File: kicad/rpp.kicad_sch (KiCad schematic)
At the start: 13 parts, among them J1 SolderPad, J2 SolderPad, J3 SolderPad, J4 SolderPad, Q1 CSD19537Q3, U1 LM5050-1

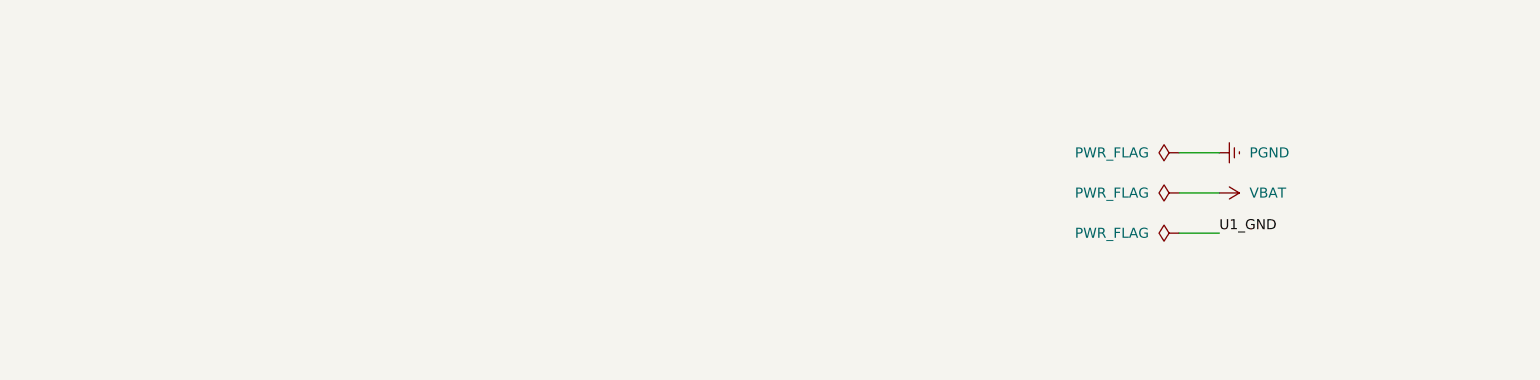
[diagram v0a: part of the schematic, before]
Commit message: Adjusted licensing for club
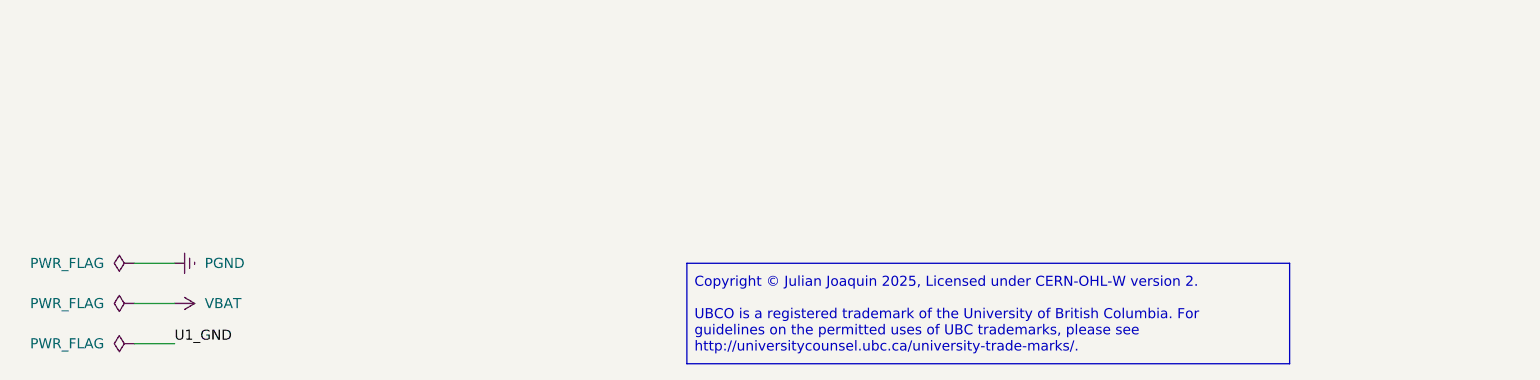
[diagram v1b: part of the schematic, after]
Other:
- company: Author: Julian Joaquin -> UBCO Aerospace Club
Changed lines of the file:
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@@
 		(date "2025-11-08")
 		(rev "D")
-		(company "Author: Julian Joaquin")
-		(comment 1 "Licensed under CERN-OHL-W version 2")
-		(comment 2 "Copyright © Julian Joaquin, 2025")
+		(company "UBCO Aerospace Club")
+		(comment 1 "Author(s): Julian Joaquin")
 		(comment 4 "A 12S battery eliminator circuit (BEC) for UAS applications.")
 	)
@@
 		)
 	)
+	(text_box "Copyright © Julian Joaquin 2025, Licensed under CERN-OHL-W version 2.\n\nUBCO is a registered trademark of the University of British Columbia. For guidelines on the permitted uses of UBC trademarks, please see http://universitycounsel.ubc.ca/university-trade-marks/."
+		(exclude_from_sim no)
+		(at 99.06 182.88 0)
+		(size 76.2 12.7)
+		(margins 0.9525 0.9525 0.9525 0.9525)
+		(stroke
+			(width 0)
+			(type solid)
+			(color 132 0 0 1)
+		)
+		(fill
+			(type none)
+		)
+		(effects
+			(font
+				(size 1.27 1.27)
+				(color 132 0 0 1)
+			)
+			(justify left)
+			(href "http://universitycounsel.ubc.ca/university-trade-marks/")
+		)
+	)
 	(junction
 		(at 173.99 78.74)
@@
 	(wire
 		(pts
-			(xy 161.29 179.07) (xy 166.37 179.07)
+			(xy 29.21 193.04) (xy 34.29 193.04)
 		)
 		(stroke
@@
 	(wire
 		(pts
-			(xy 161.29 168.91) (xy 166.37 168.91)
+			(xy 29.21 182.88) (xy 34.29 182.88)
 		)
 		(stroke
@@
 	(wire
 		(pts
-			(xy 161.29 173.99) (xy 166.37 173.99)
+			(xy 29.21 187.96) (xy 34.29 187.96)
 		)
 		(stroke
@@
 	)
 	(label "U1_GND"
-		(at 166.37 179.07 0)
+		(at 34.29 193.04 0)
 		(effects
 			(font
@@
 	(symbol
 		(lib_id "power:Earth")
-		(at 166.37 168.91 90)
+		(at 34.29 182.88 90)
 		(unit 1)
 		(exclude_from_sim no)
@@
 		(fields_autoplaced yes)
 		(property "Reference" "#PWR023"
-			(at 172.72 168.91 0)
+			(at 40.64 182.88 0)
 			(effects
 				(font
@@
 		)
 		(property "Value" "PGND"
-			(at 170.18 168.91 90)
+			(at 38.1 182.88 90)
 			(effects
 				(font
@@
 		)
 		(property "Footprint" ""
-			(at 166.37 168.91 0)
+			(at 34.29 182.88 0)
 			(effects
 				(font
@@
 		)
 		(property "Datasheet" "~"
-			(at 166.37 168.91 0)
+			(at 34.29 182.88 0)
 			(effects
 				(font
@@
 		)
 		(property "Description" "Power symbol creates a global label with name \"Earth\""
-			(at 166.37 168.91 0)
+			(at 34.29 182.88 0)
 			(effects
 				(font
@@
 	(symbol
 		(lib_id "power:PWR_FLAG")
-		(at 161.29 173.99 90)
+		(at 29.21 187.96 90)
 		(unit 1)
 		(exclude_from_sim no)
@@
 		(fields_autoplaced yes)
 		(property "Reference" "#FLG02"
-			(at 159.385 173.99 0)
+			(at 27.305 187.96 0)
 			(effects
 				(font
@@
 		)
 		(property "Value" "PWR_FLAG"
-			(at 157.48 173.99 90)
+			(at 25.4 187.96 90)
 			(effects
 				(font
@@
 		)
 		(property "Footprint" ""
-			(at 161.29 173.99 0)
+			(at 29.21 187.96 0)
 			(effects
 				(font
@@
 		)
 		(property "Datasheet" "~"
-			(at 161.29 173.99 0)
+			(at 29.21 187.96 0)
 			(effects
 				(font
@@
 		)
 		(property "Description" "Special symbol for telling ERC where power comes from"
-			(at 161.29 173.99 0)
+			(at 29.21 187.96 0)
 			(effects
 				(font
@@
 	(symbol
 		(lib_id "power:PWR_FLAG")
-		(at 161.29 168.91 90)
+		(at 29.21 182.88 90)
 		(unit 1)
 		(exclude_from_sim no)
@@
 		(fields_autoplaced yes)
 		(property "Reference" "#FLG06"
-			(at 159.385 168.91 0)
+			(at 27.305 182.88 0)
 			(effects
 				(font
@@
 		)
 		(property "Value" "PWR_FLAG"
-			(at 157.48 168.91 90)
+			(at 25.4 182.88 90)
 			(effects
 				(font
@@
 		)
 		(property "Footprint" ""
-			(at 161.29 168.91 0)
+			(at 29.21 182.88 0)
 			(effects
 				(font
@@
 		)
 		(property "Datasheet" "~"
-			(at 161.29 168.91 0)
+			(at 29.21 182.88 0)
 			(effects
 				(font
@@
 		)
 		(property "Description" "Special symbol for telling ERC where power comes from"
-			(at 161.29 168.91 0)
+			(at 29.21 182.88 0)
 			(effects
 				(font
@@
 	(symbol
 		(lib_id "power:VDDA")
-		(at 166.37 173.99 270)
+		(at 34.29 187.96 270)
 		(unit 1)
 		(exclude_from_sim no)
@@
 		(dnp no)
 		(property "Reference" "#PWR018"
-			(at 162.56 173.99 0)
+			(at 30.48 187.96 0)
 			(effects
 				(font
@@
 		)
 		(property "Value" "VBAT"
-			(at 170.18 173.99 90)
+			(at 38.1 187.96 90)
 			(effects
 				(font
@@
 		)
 		(property "Footprint" ""
-			(at 166.37 173.99 0)
+			(at 34.29 187.96 0)
 			(effects
 				(font
@@
 		)
 		(property "Datasheet" ""
-			(at 166.37 173.99 0)
+			(at 34.29 187.96 0)
 			(effects
 				(font
@@
 		)
 		(property "Description" "Power symbol creates a global label with name \"VDDA\""
-			(at 166.37 173.99 0)
+			(at 34.29 187.96 0)
 			(effects
 				(font
@@
 	(symbol
 		(lib_id "power:PWR_FLAG")
-		(at 161.29 179.07 90)
+		(at 29.21 193.04 90)
 		(unit 1)
 		(exclude_from_sim no)
@@
 		(fields_autoplaced yes)
 		(property "Reference" "#FLG08"
-			(at 159.385 179.07 0)
+			(at 27.305 193.04 0)
 			(effects
 				(font
@@
 		)
 		(property "Value" "PWR_FLAG"
-			(at 157.48 179.07 90)
+			(at 25.4 193.04 90)
 			(effects
 				(font
@@
 		)
 		(property "Footprint" ""
-			(at 161.29 179.07 0)
+			(at 29.21 193.04 0)
 			(effects
 				(font
@@
 		)
 		(property "Datasheet" "~"
-			(at 161.29 179.07 0)
+			(at 29.21 193.04 0)
 			(effects
 				(font
@@
 		)
 		(property "Description" "Special symbol for telling ERC where power comes from"
-			(at 161.29 179.07 0)
-			(effects
-				(font
+			(at 29.21 193.04 0)
+			(effects
+				(font
